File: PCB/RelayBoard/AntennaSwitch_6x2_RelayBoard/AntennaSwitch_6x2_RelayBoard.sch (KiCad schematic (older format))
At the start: 34 parts, among them J1 Conn_Coaxial, J10 Conn_01x08, J2 Conn_Coaxial, J3 Conn_Coaxial, J4 Conn_Coaxial, J5 Conn_Coaxial, J6 Conn_Coaxial, J7 Conn_Coaxial, J8 Conn_Coaxial, J9 Conn_01x08, K1 FINDER-40.61, K10 FINDER-40.61, K11 FINDER-40.61, K12 FINDER-40.61, K13 FINDER-40.61, K14 FINDER-40.61, K15 FINDER-40.61, K16 FINDER-40.61, K17 FINDER-40.61, K18 FINDER-40.61, K2 FINDER-40.61, K3 FINDER-40.61, K4 FINDER-40.61, K5 FINDER-40.61, K6 FINDER-40.61, K7 FINDER-40.61, K8 FINDER-40.61, K9 FINDER-40.61, U1 ULN2003, U2 ULN2003, U3 74HC04, U4 74HC04

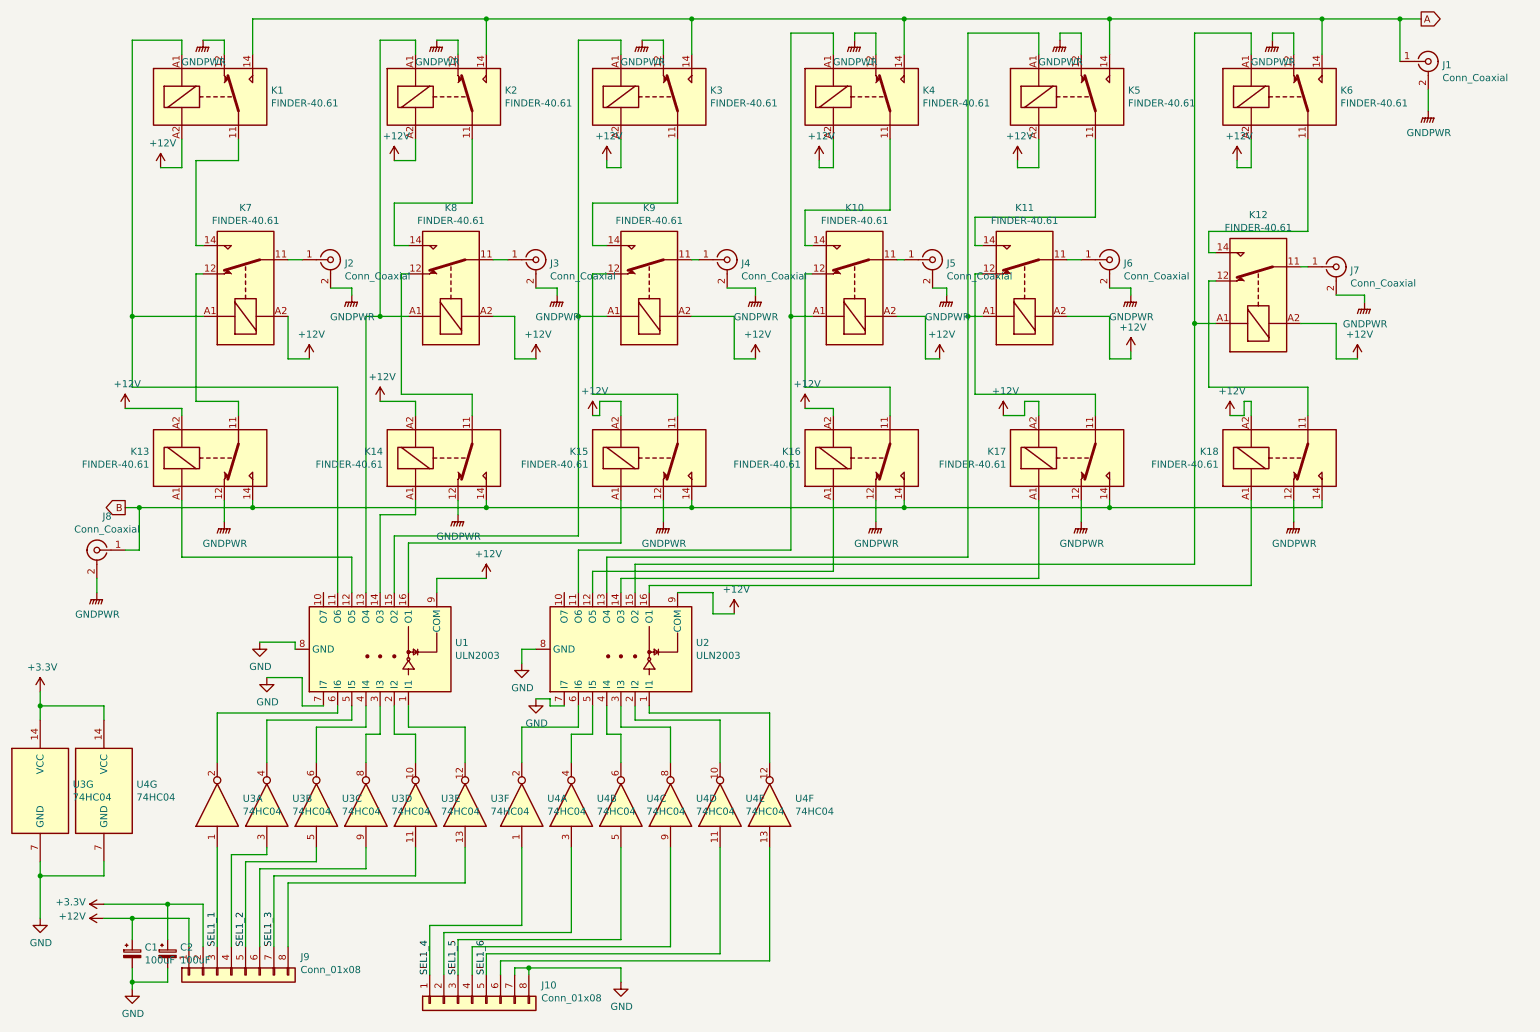
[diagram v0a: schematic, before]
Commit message: New control board design
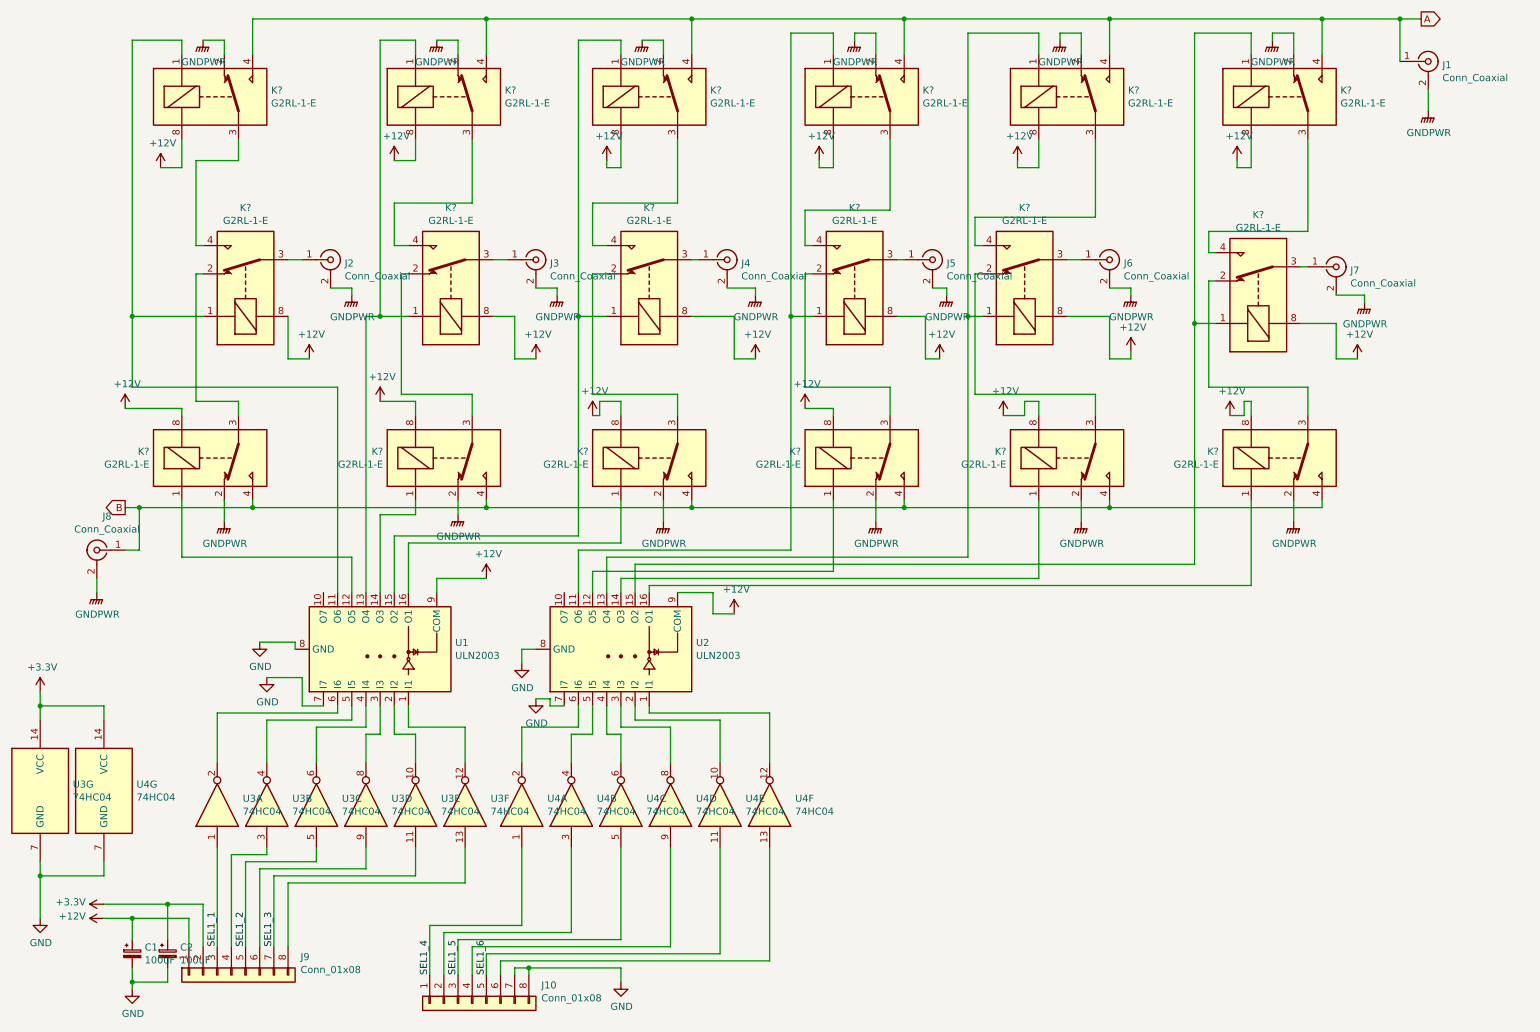
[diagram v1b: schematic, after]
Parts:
- removed K1, K10, K11, K12, K13, K14, K15, K16, K17, K18, K2, K3, K4, K5, K6, K7, K8, K9: FINDER-40.61, MyPCBLib:Finder_40.61, symbol MySchLib:FINDER-40.61
- added K? (x18): G2RL-1-E, symbol MySchLib:G2RL-1-E
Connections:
- net +12V: now also K?.8, K?.8, K?.8, K?.8, K?.8, K?.8, K?.8, K?.8, K?.8, K?.8, K?.8, K?.8, K?.8, K?.8, K?.8, K?.8, K?.8, K?.8
- net A: now also K?.4, K?.4, K?.4, K?.4, K?.4, K?.4, K?.5, K?.5, K?.5, K?.5, K?.5, K?.5
- net B: now also K?.4, K?.4, K?.4, K?.4, K?.4, K?.4, K?.5, K?.5, K?.5, K?.5, K?.5, K?.5
- net GNDPWR: now also K?.2, K?.2, K?.2, K?.2, K?.2, K?.2, K?.2, K?.2, K?.2, K?.2, K?.2, K?.2, K?.7, K?.7, K?.7, K?.7, K?.7, K?.7, K?.7, K?.7, K?.7, K?.7, K?.7, K?.7
- net at J2.1 (In): now also K?.3, K?.6
- net at U1.11 (O6): now also K?.1, K?.1
- net at J3.1 (In): now also K?.3, K?.6
- net at U1.13 (O4): now also K?.1, K?.1
- net at J4.1 (In): now also K?.3, K?.6
- net at U1.15 (O2): now also K?.1, K?.1
- net at J5.1 (In): now also K?.3, K?.6
- net at U2.11 (O6): now also K?.1, K?.1
- net at J6.1 (In): now also K?.3, K?.6
- net at U2.13 (O4): now also K?.1, K?.1
- net at J7.1 (In): now also K?.3, K?.6
- net at U2.15 (O2): now also K?.1, K?.1
- net at U1.12 (O5): now also K?.1
- net at U1.14 (O3): now also K?.1
- net at U1.16 (O1): now also K?.1
- net at U2.12 (O5): now also K?.1
- net at U2.14 (O3): now also K?.1
- net at U2.16 (O1): now also K?.1
- new net: K?.3, K?.4, K?.5, K?.6 (x6)
- new net: K?.2, K?.3, K?.6, K?.7 (x6)
